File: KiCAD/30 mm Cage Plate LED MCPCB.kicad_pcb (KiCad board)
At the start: 2 copper layers, 40 x 40 mm, 27 parts, among them IC1 AL8843QSP-13, J1 Conn_01x08_Socket, J2 0, U2 TLP3480, U3 TLP3480, U4 TLP3480, U5 TLP3480, U6 SN74LVC1G139DCUR

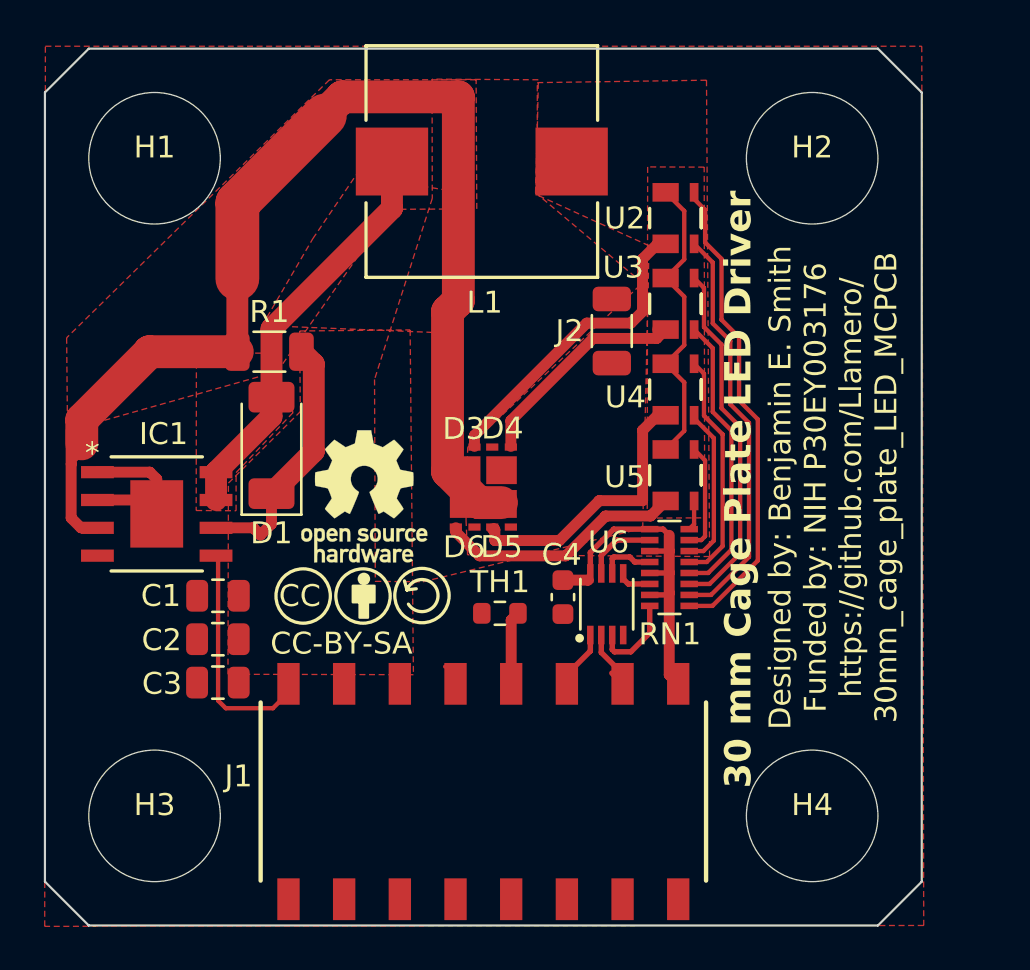
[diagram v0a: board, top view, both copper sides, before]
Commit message: Add pmos array mux
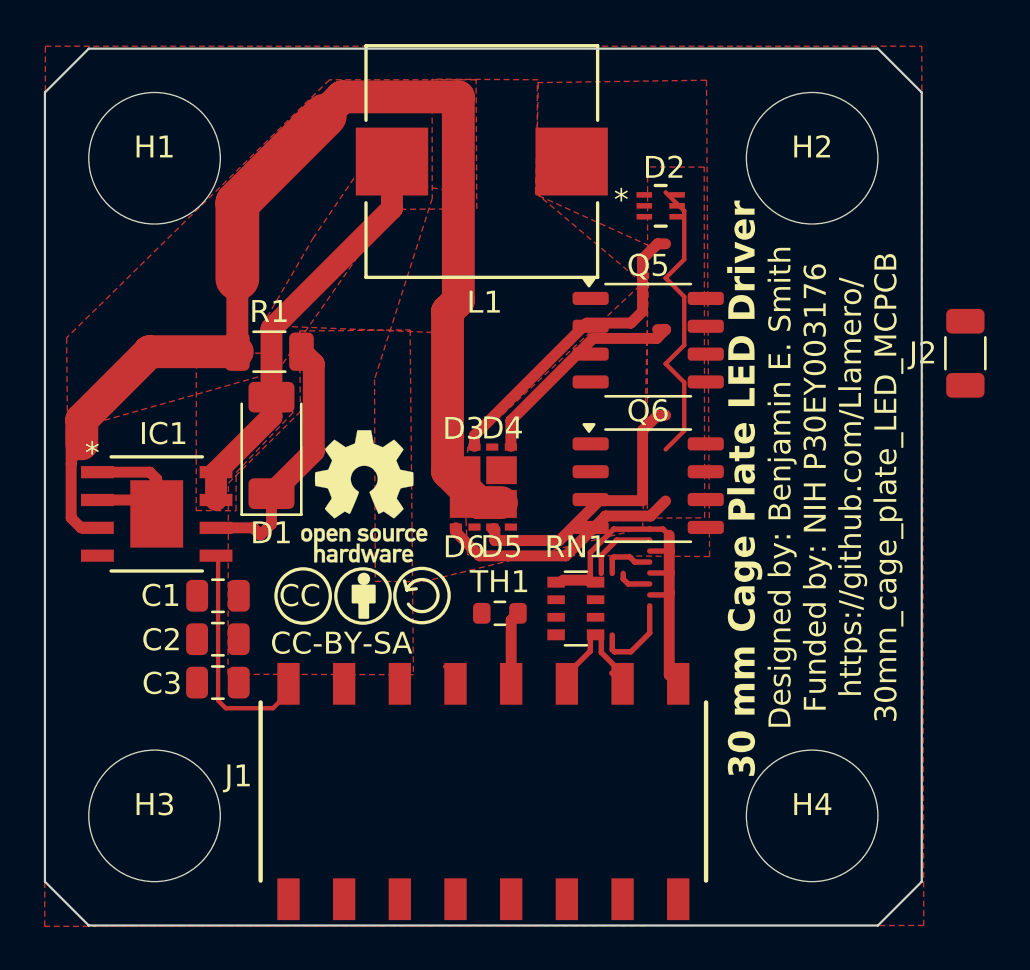
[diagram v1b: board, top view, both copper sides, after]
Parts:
- removed C4: 0.1μF, Capacitor_SMD:C_0603_1608Metric
- removed U2, U3, U4, U5: TLP3480, Custom:TLP3480-SSR
- removed U6: SN74LVC1G139DCUR, Custom:SOP50P310X90-8N
- added D2: D_Zener, Custom:DFN6_TDS3011_SEM, F.Cu at (128.1, 67.2)
- added Q5: 2x_p-channel, Custom:SOP-8_3.9x4.9mm_P1.27mm, F.Cu at (127.5, 73.3)
- added Q6: 2x_p-channel, Custom:SOP-8_3.9x4.9mm_P1.27mm, F.Cu at (127.5, 79.9)
- L1: value 47μH -> 15μH
- RN1: value 180 -> 2200; footprint Resistor_SMD:R_Array_Convex_8x0602 -> Resistor_SMD:R_Array_Convex_4x0603
- moved J2 16.2 mm to (142.0, 73.9)
- moved RN1 4.66 mm to (124.2, 85.5), turned to 0 degrees
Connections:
- J1 pad 4: GND -> /Temp
- J1 pad 5: /Temp -> /4
- J1 pad 6: /A -> /3
- J1 pad 7: /B -> /2
- J1 pad 8: /5V -> /1
- RN1 pad 1: Net-(RN1-R1.1) -> /LED+
- RN1 pad 2: Net-(RN1-R2.1) -> /LED+
- RN1 pad 3: Net-(RN1-R3.1) -> /LED+
- RN1 pad 4: Net-(RN1-R4.1) -> /LED+
- RN1 pad 5: Net-(RN1-R5.1) -> /4
- RN1 pad 6: Net-(RN1-R6.1) -> /3
- RN1 pad 7: Net-(RN1-R7.1) -> /2
- RN1 pad 8: Net-(RN1-R8.1) -> /1
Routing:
- net Net-(RN1-R1.1): track 22.0 -> 0.00 mm
- net Net-(RN1-R2.1): track 18.8 -> 0.00 mm
- net Net-(RN1-R3.1): track 16.3 -> 0.00 mm
- net /5V: track 16.3 -> 0.00 mm
- net /1: track 3.32 -> 19.6 mm
- net /LED+: track 55.3 -> 69.1 mm
- net /LED-: track 13.8 -> 0.00 mm
- net Net-(RN1-R4.1): track 13.1 -> 0.00 mm
- net Net-(RN1-R5.1): track 10.7 -> 0.00 mm
- net Net-(RN1-R6.1): track 7.41 -> 0.00 mm
- net Net-(RN1-R7.1): track 4.96 -> 0.00 mm
- net /B: track 3.32 -> 0.00 mm
- net /2: track 2.51 -> 5.84 mm
- net /3: track 1.56 -> 4.23 mm
- net /A: track 2.67 -> 0.00 mm
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
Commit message: pmos mux connected - better conduction path
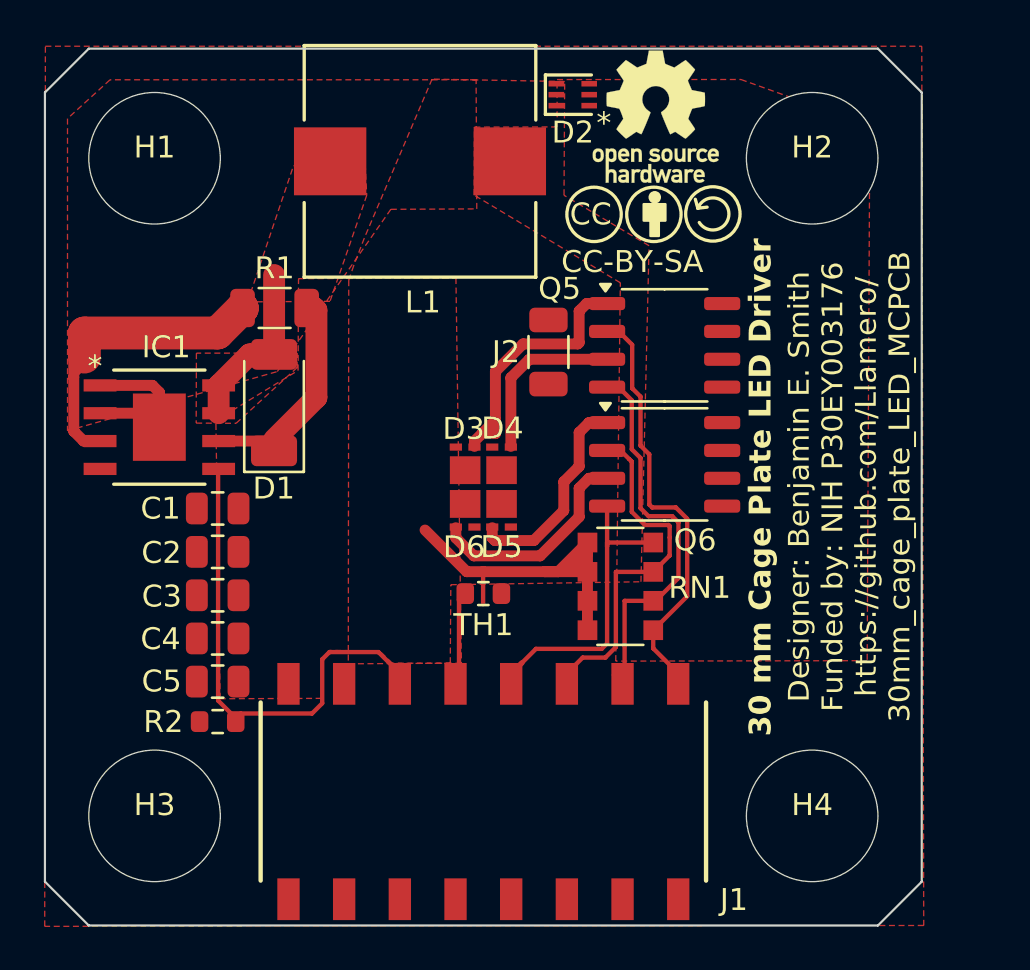
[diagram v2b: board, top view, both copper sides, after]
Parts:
- added C4: 22μF, Capacitor_SMD:C_0805_2012Metric, F.Cu at (107.9, 86.9)
- added C5: 22μF, Capacitor_SMD:C_0805_2012Metric, F.Cu at (107.9, 88.9)
- added R2: 4700, Resistor_SMD:R_0603_1608Metric, F.Cu at (107.9, 90.7)
- RN1: value 2200 -> 4700; footprint Resistor_SMD:R_Array_Convex_4x0603 -> Resistor_SMD:R_Array_Convex_4x1206
- moved SYM2 21.9 mm to (127.9, 67.3)
- moved SYM1 21.8 mm to (127.9, 63.1)
- moved J2 19.0 mm to (123.0, 73.8), turned to -90 degrees
- moved D2 6.46 mm to (124.1, 62.1), turned to 180 degrees
- moved C1 3.98 mm to (107.9, 81.0)
- moved C2 3.98 mm to (107.9, 83.0)
- moved C3 3.98 mm to (107.9, 84.9)
- moved IC1 3.96 mm to (105.2, 77.3)
- moved L1 2.82 mm to (117.1, 65.1)
- moved RN1 2.27 mm to (126.2, 84.5)
- moved R1 2.01 mm to (110.5, 71.8)
- moved D1 1.95 mm to (110.5, 76.1)
- moved Q6 1.23 mm to (128.3, 79.0)
- moved TH1 1.17 mm to (120.0, 84.9), turned to 180 degrees
- moved Q5 0.79 mm to (128.3, 73.5)
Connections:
- J1 pad 1: /PWM -> /Vin
- J1 pad 3: /Vin -> /PWM
- RN1 pad 5: /4 -> /1
- RN1 pad 6: /3 -> /2
- RN1 pad 7: /2 -> /3
- RN1 pad 8: /1 -> /4
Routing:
- net /LED+: track 69.1 -> 32.7 mm
- net /3: track 4.23 -> 16.9 mm
- net /2: track 5.84 -> 18.3 mm
- net /PWM: track 11.2 -> 22.9 mm
- net Net-(D1-A): track 18.8 -> 7.50 mm
- net /4: track 4.00 -> 14.2 mm
- net Net-(D5-K): track 12.7 -> 9.66 mm
- net Net-(D4-K): track 10.3 -> 7.87 mm
- net Net-(D3-K): track 14.2 -> 12.2 mm
- net /1: track 19.6 -> 20.9 mm
- net Net-(D6-K): track 11.3 -> 9.94 mm
- net /Vin: track 11.8 -> 10.7 mm
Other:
- board text added: "Designer: Benjamin E. Smith Funded by: NIH P30EY003176 https://github.com/Llamero/ 30mm_cage_plate_LED_MCPCB"
- board text removed: "Designed by: Benjamin E. Smith Funded by: NIH P30EY003176 https://github.com/Llamero/ 30mm_cage_plate_LED_MCPCB"
